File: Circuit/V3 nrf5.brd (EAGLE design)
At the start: 45.1 x 52.7 mm, 55 parts, among them J4 USB Micro, J7 CORTEX_DEBUG_SMD, Q2 BSS84, U2 MCP73831, U3 BC840M, U4 MIC5317 (MIC5205), U5 74AHCT2G125, U8 TPS61235P, Y2 FC-12M

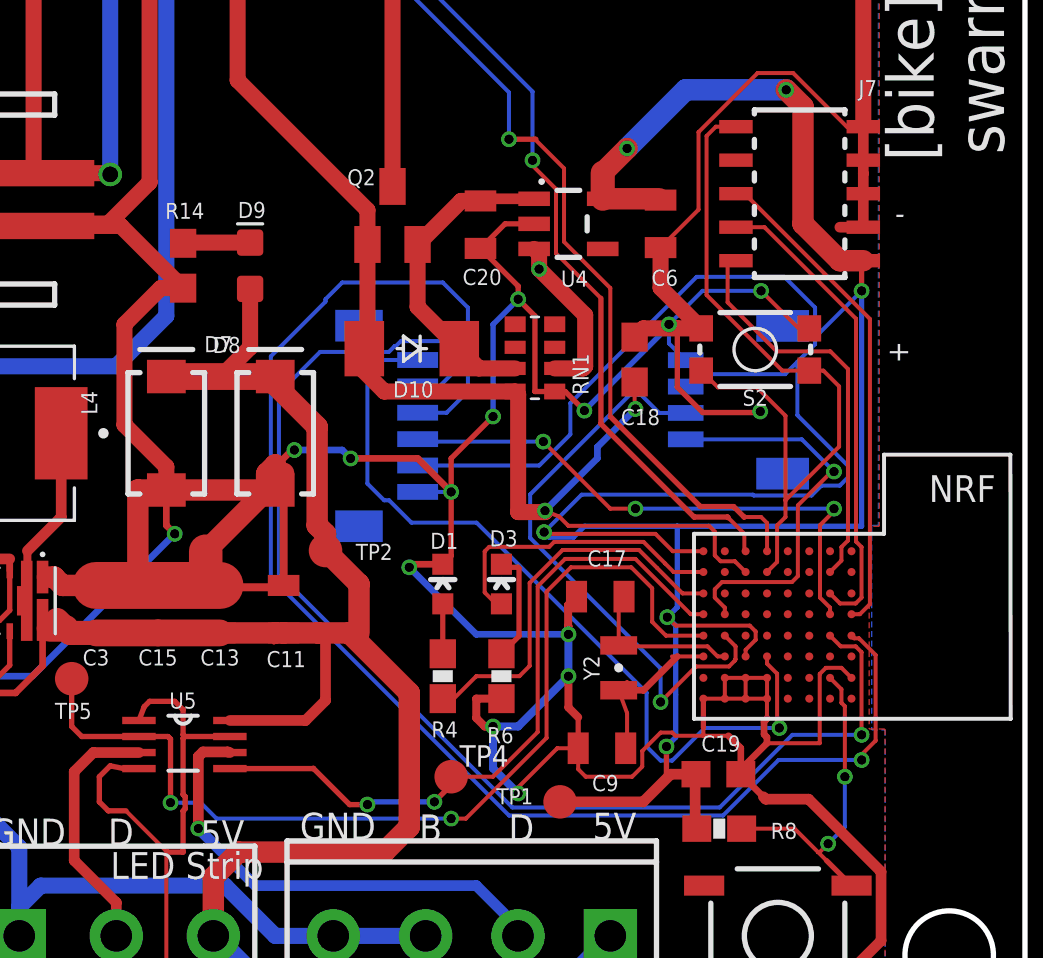
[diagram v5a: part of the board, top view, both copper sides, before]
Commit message: fix traces gnd
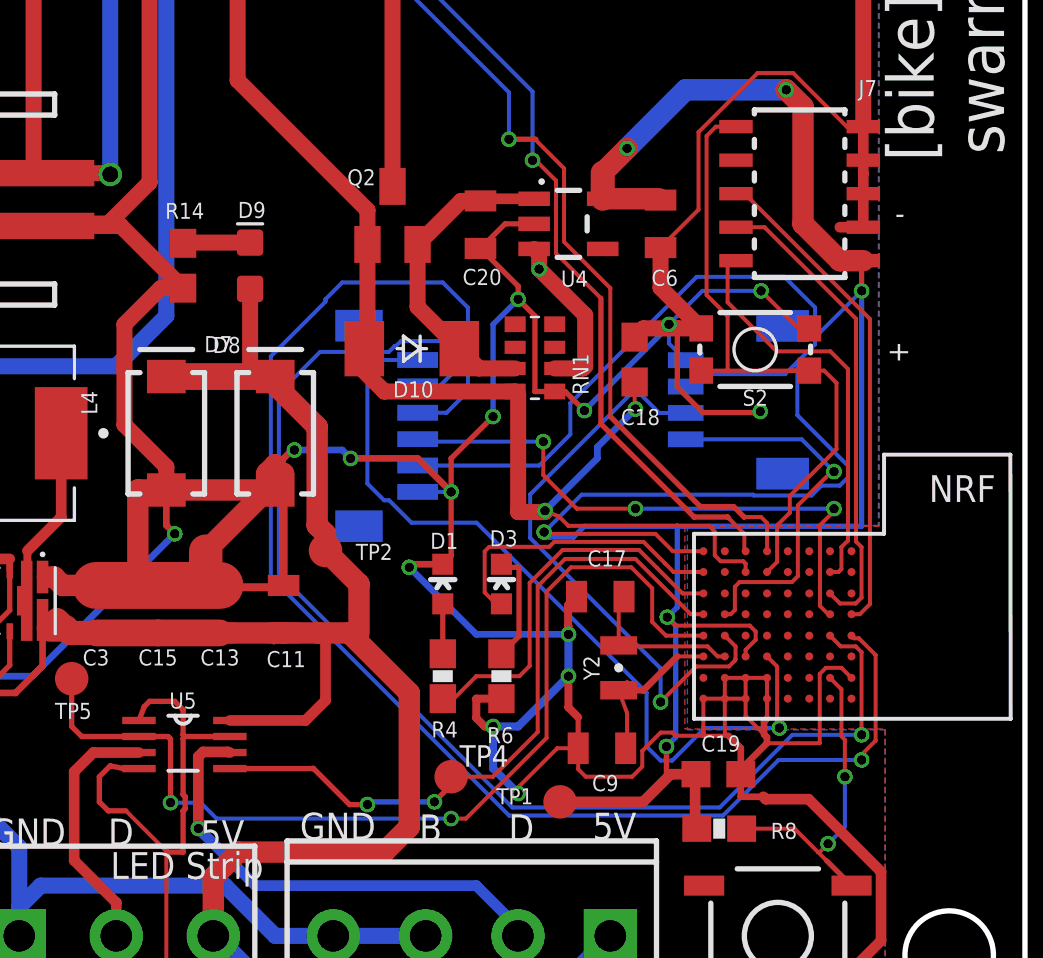
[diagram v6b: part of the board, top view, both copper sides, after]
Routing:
- net RESET: track 29.3 -> 24.8 mm
- net GND: track 338.8 -> 341.7 mm
- net PIN_01: track 21.4 -> 22.2 mm
- net 5V: track 90.5 -> 91.2 mm
- net SCL: track 15.6 -> 15.0 mm

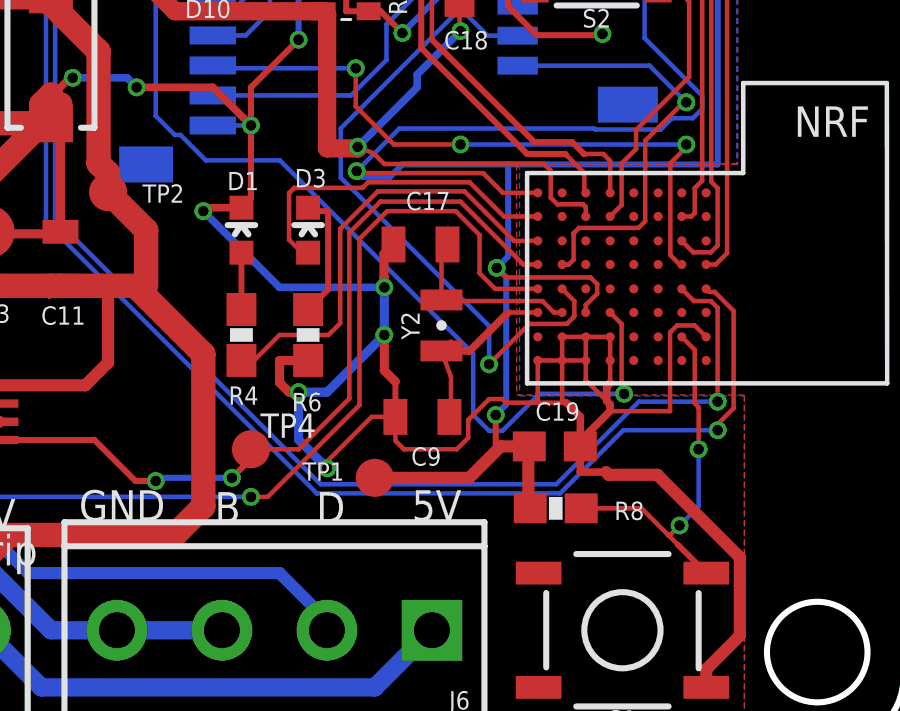
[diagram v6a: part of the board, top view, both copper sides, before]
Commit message: Moving to nrf52840-DK BSP pins for buttons and leds. Also driving LEDs with active LOW.
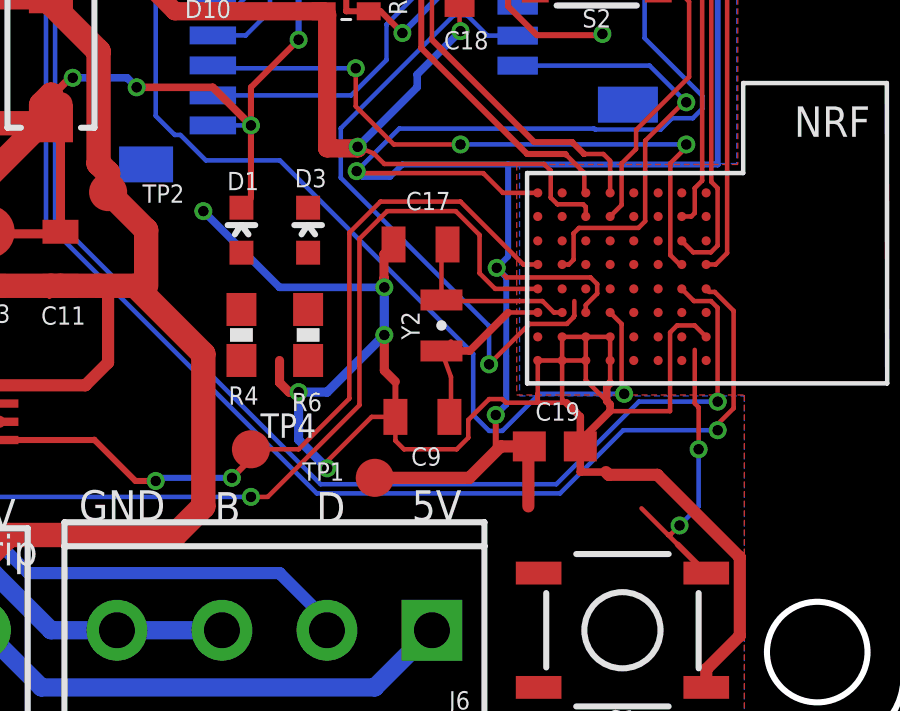
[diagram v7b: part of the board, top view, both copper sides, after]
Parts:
- removed R8: 10k, SparkFun:0603-RES
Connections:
- removed net N$7: D3.C, R6.2
- new net N$8: D3.A, R6.1
- net 3.3V: now also R4.1, R6.2; no longer R8.1
- net GND: no longer D1.C, R6.1
- net LED_1: now also D1.C, U3.D4; no longer R4.1, U3.C7
- net LED_2: now also D3.C, U3.C4; no longer D3.A, U3.B7
- net SWITCH_1: no longer R8.2, U3.G1
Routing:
- net LED_1: track 14.7 -> 0.00 mm
- net LED_2: track 11.3 -> 0.00 mm
- net N$7: track 4.25 -> 0.00 mm
- net SWITCH_1: track 12.4 -> 9.74 mm
- net GND: track 341.7 -> 339.1 mm
- net N$1: track 1.89 -> 0.00 mm
- net SDA: track 22.2 -> 21.7 mm
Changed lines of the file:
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@@
 <drawing>
 <settings>
-<setting alwaysvectorfont="no"/>
+<setting alwaysvectorfont="yes"/>
 <setting keepoldvectorfont="yes"/>
 <setting verticaltext="up"/>
@@
 <attribute name="VALUE" x="31.75" y="6.7945" size="0.6096" layer="27" font="vector" ratio="20" rot="R180" align="top-center"/>
 </element>
-<element name="R8" library="SparkFun" package="0603-RES" value="10k" x="29.5275" y="8.1915" smashed="yes">
-<attribute name="DIGIKEY" value="P10KGCT-ND" x="29.5275" y="8.1915" size="1.778" layer="27" display="off"/>
-<attribute name="NAME" x="32.48025" y="8.41375" size="0.6096" layer="25" font="vector" rot="R180"/>
-<attribute name="VALUE" x="28.5115" y="7.0485" size="0.4064" layer="27" font="vector"/>
-</element>
 <element name="U3" library="BC840M-v1" package="BC840M" value="BC840M" x="28.575" y="19.3675" smashed="yes" rot="R270">
 <attribute name="DIGIKEY" value="1914-BC840MCT-ND" x="28.575" y="19.3675" size="1.778" layer="27" rot="R270" display="off"/>
@@
 <contactref element="U3" pad="G0"/>
 <contactref element="C19" pad="2"/>
-<contactref element="D1" pad="C"/>
-<contactref element="R6" pad="1"/>
 <contactref element="C20" pad="2"/>
 <contactref element="RN1" pad="1"/>
@@
 <wire x1="20.6375" y1="12.065" x2="20.32" y2="12.3825" width="0.3048" layer="1"/>
 <wire x1="20.32" y1="13.12" x2="20.32" y2="12.3825" width="0.3048" layer="1"/>
-<wire x1="20.32" y1="13.12" x2="21.2725" y2="13.12" width="0.3048" layer="1"/>
 <wire x1="20.955" y1="12.065" x2="20.955" y2="10.4775" width="0.3048" layer="16"/>
 <wire x1="20.955" y1="10.4775" x2="21.9075" y2="9.525" width="0.3048" layer="16"/>
@@
 <wire x1="32.33053125" y1="36.83" x2="30.9822125" y2="36.83" width="0.1524" layer="1"/>
 <wire x1="30.9822125" y1="36.83" x2="28.7432" y2="34.5909875" width="0.1524" layer="1"/>
-<wire x1="19.05" y1="18.2125" x2="19.3675" y2="18.53" width="0.2032" layer="1"/>
 <wire x1="19.3675" y1="20.955" x2="19.3675" y2="18.53" width="0.2032" layer="1"/>
 <wire x1="19.3675" y1="20.955" x2="19.3675" y2="22.225" width="0.2032" layer="1"/>
@@
 <via x="17.78" y="18.0975" extent="1-16" drill="0.35"/>
 <wire x1="17.78" y1="18.0975" x2="17.895" y2="18.2125" width="0.254" layer="1"/>
-<wire x1="17.895" y1="18.2125" x2="19.05" y2="18.2125" width="0.254" layer="1"/>
 <wire x1="7.4931" y1="50.7752625" x2="7.4931" y2="51.05684375" width="0.254" layer="1"/>
 <wire x1="7.4931" y1="51.05684375" x2="6.16244375" y2="52.3875" width="0.254" layer="1"/>
@@
 <wire x1="29.7402" y1="13.1191" x2="29.7402" y2="11.8174" width="0.1524" layer="1"/>
 <wire x1="29.7402" y1="11.8174" x2="29.845" y2="11.7126" width="0.1524" layer="1"/>
+<wire x1="19.3675" y1="18.53" x2="17.895" y2="18.2125" width="0" layer="19" extent="1-1"/>
 </signal>
 <signal name="RESET">
@@
 <wire x1="30.4916125" y1="32.258" x2="35.2397" y2="27.5099125" width="0.1524" layer="1"/>
 <wire x1="35.2397" y1="27.5099125" x2="35.2397" y2="16.7009" width="0.1524" layer="1"/>
-</signal>
-<signal name="LED_1">
-<contactref element="U3" pad="C7"/>
-<contactref element="R4" pad="1"/>
-<wire x1="28.9274" y1="17.1069" x2="28.13685" y2="17.1069" width="0.1524" layer="1"/>
-<wire x1="28.13685" y1="17.1069" x2="27.1699" y2="18.07385" width="0.1524" layer="1"/>
-<wire x1="27.1699" y1="18.07385" x2="26.4891" y2="18.75465" width="0.1524" layer="1"/>
-<wire x1="26.4891" y1="18.75465" x2="23.59330625" y2="18.75465" width="0.1524" layer="1"/>
-<wire x1="23.59330625" y1="18.75465" x2="22.3421" y2="17.50344375" width="0.1524" layer="1"/>
-<wire x1="22.3421" y1="17.50344375" x2="22.3421" y2="14.35940625" width="0.1524" layer="1"/>
-<wire x1="21.95269375" y1="13.97" x2="20.32" y2="13.97" width="0.1524" layer="1"/>
-<wire x1="20.32" y1="13.97" x2="19.47" y2="13.12" width="0.1524" layer="1"/>
-<wire x1="19.47" y1="13.12" x2="19.05" y2="13.12" width="0.1524" layer="1"/>
-<wire x1="22.3421" y1="14.35940625" x2="21.95269375" y2="13.97" width="0.1524" layer="1"/>
 </signal>
 <signal name="STRIP_5V">
@@
 <signal name="SWITCH_1">
 <contactref element="S1" pad="3"/>
-<contactref element="R8" pad="2"/>
 <wire x1="33.5915" y1="6.985" x2="34.544" y2="6.0325" width="0.2" layer="1"/>
-<contactref element="U3" pad="G1"/>
 <wire x1="34.1598" y1="11.6912875" x2="34.29" y2="11.5610875" width="0.1524" layer="1"/>
-<wire x1="33.728" y1="13.9065" x2="34.1598" y2="13.4747" width="0.1524" layer="1"/>
 <wire x1="34.1598" y1="13.4747" x2="34.1598" y2="11.6912875" width="0.1524" layer="1"/>
 <wire x1="34.29" y1="11.5610875" x2="34.29" y2="10.16" width="0.1524" layer="1"/>
 <via x="34.29" y="10.16" extent="1-16" drill="0.35"/>
-<wire x1="30.3775" y1="8.1915" x2="32.385" y2="8.1915" width="0.1524" layer="1"/>
 <wire x1="32.385" y1="8.1915" x2="33.274" y2="7.3025" width="0.1524" layer="1"/>
 <wire x1="33.274" y1="7.3025" x2="33.5915" y2="6.985" width="0.1524" layer="1"/>
@@
 </signal>
 <signal name="LED_2">
-<contactref element="D3" pad="A"/>
-<contactref element="U3" pad="B7"/>
-<wire x1="28.9274" y1="17.9197" x2="27.8003" y2="17.9197" width="0.1524" layer="1"/>
-<wire x1="27.8003" y1="17.9197" x2="27.4747" y2="18.2453" width="0.1524" layer="1"/>
-<wire x1="27.4747" y1="18.2453" x2="26.66055" y2="19.05945" width="0.1524" layer="1"/>
-<wire x1="26.66055" y1="19.05945" x2="23.2705875" y2="19.05945" width="0.1524" layer="1"/>
-<wire x1="20.8095625" y1="18.87285" x2="20.6375" y2="18.7007875" width="0.1524" layer="1"/>
-<wire x1="20.6375" y1="18.7007875" x2="20.6375" y2="17.145" width="0.1524" layer="1"/>
-<wire x1="23.2705875" y1="19.05945" x2="23.0839875" y2="18.87285" width="0.1524" layer="1"/>
-<wire x1="23.0839875" y1="18.87285" x2="20.8095625" y2="18.87285" width="0.1524" layer="1"/>
-<wire x1="20.6375" y1="17.145" x2="21.07" y2="16.7125" width="0.1524" layer="1"/>
-<wire x1="21.07" y1="16.7125" x2="21.2725" y2="16.7125" width="0.1524" layer="1"/>
+<contactref element="D3" pad="C"/>
+<contactref element="U3" pad="C4"/>
+<wire x1="21.2725" y1="18.2125" x2="31.3404" y2="17.1069" width="0" layer="19" extent="1-1"/>
 </signal>
 <signal name="VBUS">
@@
 <contactref element="U4" pad="5"/>
 <contactref element="C6" pad="1"/>
-<contactref element="R8" pad="1"/>
 <contactref element="TP1" pad="TP"/>
 <contactref element="U3" pad="A7"/>
@@
 <wire x1="27.8765" y1="11.65225" x2="27.52725" y2="11.303" width="0.2032" layer="16"/>
 <wire x1="28.614" y1="10.2235" x2="28.614" y2="8.255" width="0.4064" layer="1"/>
-<wire x1="28.614" y1="8.255" x2="28.6775" y2="8.1915" width="0.4064" layer="1"/>
 <contactref element="J5" pad="2"/>
 <contactref element="J2" pad="2"/>
@@
 <wire x1="32.4894" y1="25.8811125" x2="32.4894" y2="23.8637" width="0.1524" layer="16"/>
 <wire x1="32.4894" y1="23.8637" x2="34.40785" y2="21.94525" width="0.1524" layer="16"/>
-</signal>
-<signal name="N$1">
-<contactref element="R4" pad="2"/>
-<contactref element="D1" pad="A"/>
-<wire x1="19.05" y1="14.82" x2="19.05" y2="16.7125" width="0.2" layer="1"/>
-</signal>
-<signal name="N$7">
+<contactref element="R4" pad="1"/>
 <contactref element="R6" pad="2"/>
-<contactref element="D3" pad="C"/>
-<wire x1="21.2725" y1="18.2125" x2="21.3875" y2="18.0975" width="0.2" layer="1"/>
-<wire x1="21.3875" y1="18.0975" x2="21.9075" y2="18.0975" width="0.2" layer="1"/>
-<wire x1="21.9075" y1="18.0975" x2="21.93925" y2="18.06575" width="0.2" layer="1"/>
-<wire x1="21.93925" y1="15.48675" x2="21.2725" y2="14.82" width="0.2" layer="1"/>
-<wire x1="21.93925" y1="18.06575" x2="21.93925" y2="15.48675" width="0.2" layer="1"/>
+<wire x1="19.05" y1="13.12" x2="21.2725" y2="14.82" width="0" layer="19" extent="1-1"/>
+<wire x1="22.89175" y1="19.431" x2="21.2725" y2="14.82" width="0" layer="19" extent="1-1"/>
 </signal>
 <signal name="N$4">
@@
 <signal name="SDA">
 <contactref element="J5" pad="3"/>
-<contactref element="U3" pad="E6"/>
 <wire x1="26.5722875" y1="24.62885" x2="26.1327125" y2="24.62885" width="0.1524" layer="16"/>
 <wire x1="22.36115" y1="19.2112125" x2="27.305" y2="14.2673625" width="0.1524" layer="16"/>
@@
 <wire x1="27.305" y1="14.2673625" x2="27.305" y2="12.9919" width="0.1524" layer="16"/>
 <wire x1="30.1466" y1="14.605" x2="30.1466" y2="15.1003" width="0.1524" layer="1"/>
-<wire x1="30.1466" y1="15.1003" x2="29.7402" y2="15.5067" width="0.1524" layer="1"/>
 <wire x1="28.2575" y1="23.9475" x2="27.2536375" y2="23.9475" width="0.1524" layer="16"/>
 <wire x1="27.2536375" y1="23.9475" x2="26.5722875" y2="24.62885" width="0.1524" layer="16"/>
+<contactref element="U3" pad="E6"/>
+<wire x1="30.1466" y1="15.1003" x2="29.7402" y2="15.5067" width="0" layer="19" extent="1-1"/>
 </signal>
 <signal name="SCL">
@@
 <wire x1="31.7214" y1="12.0936" x2="31.80769375" y2="12.00730625" width="0.1524" layer="1"/>
 </signal>
+<signal name="N$1">
+<contactref element="R4" pad="2"/>
+<contactref element="D1" pad="A"/>
+<wire x1="19.05" y1="14.82" x2="19.05" y2="16.7125" width="0" layer="19" extent="1-1"/>
+</signal>
+<signal name="LED_1">
+<contactref element="D1" pad="C"/>
+<contactref element="U3" pad="D4"/>
+<wire x1="19.05" y1="18.2125" x2="31.3404" y2="16.3195" width="0" layer="19" extent="1-1"/>
+</signal>
+<signal name="N$8">
+<contactref element="R6" pad="1"/>
+<contactref element="D3" pad="A"/>
+<wire x1="21.2725" y1="13.12" x2="21.2725" y2="16.7125" width="0" layer="19" extent="1-1"/>
+</signal>
 </signals>

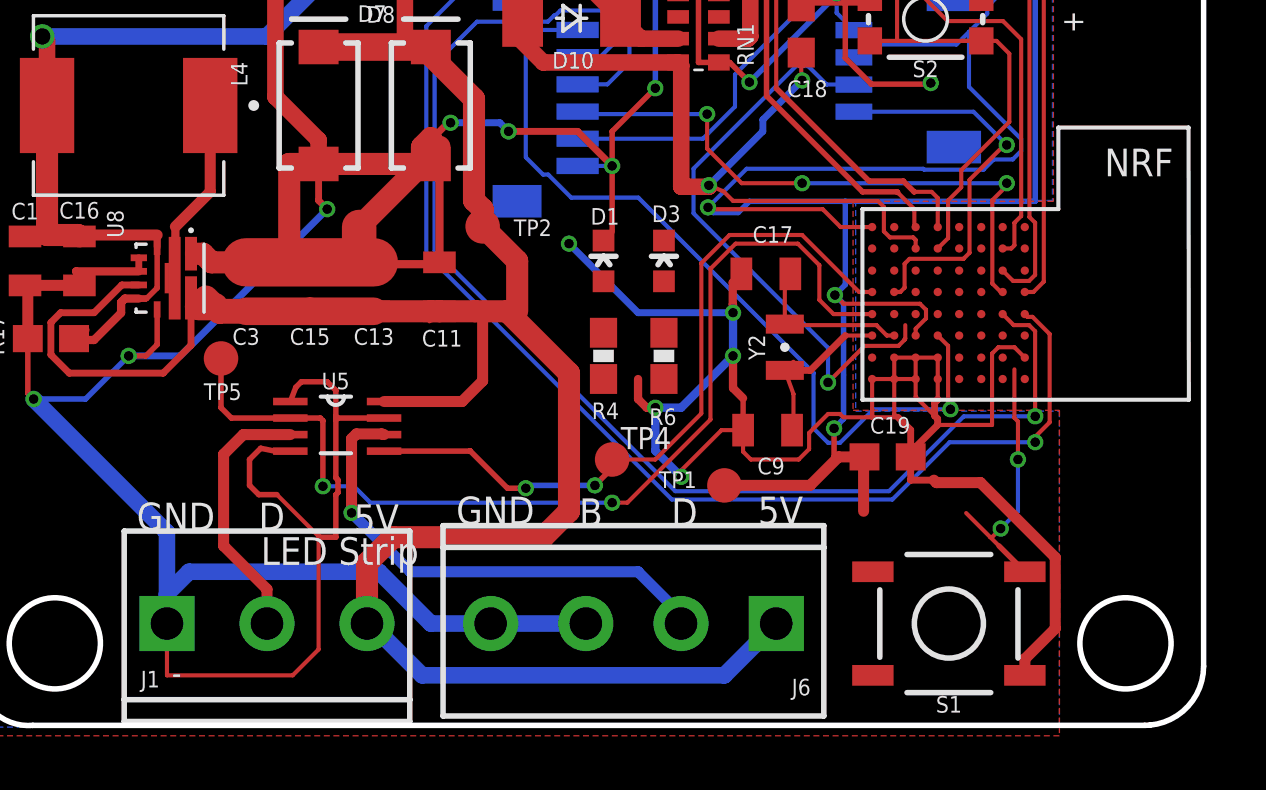
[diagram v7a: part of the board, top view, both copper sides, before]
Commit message: Adding debugging pins for switch and leds.
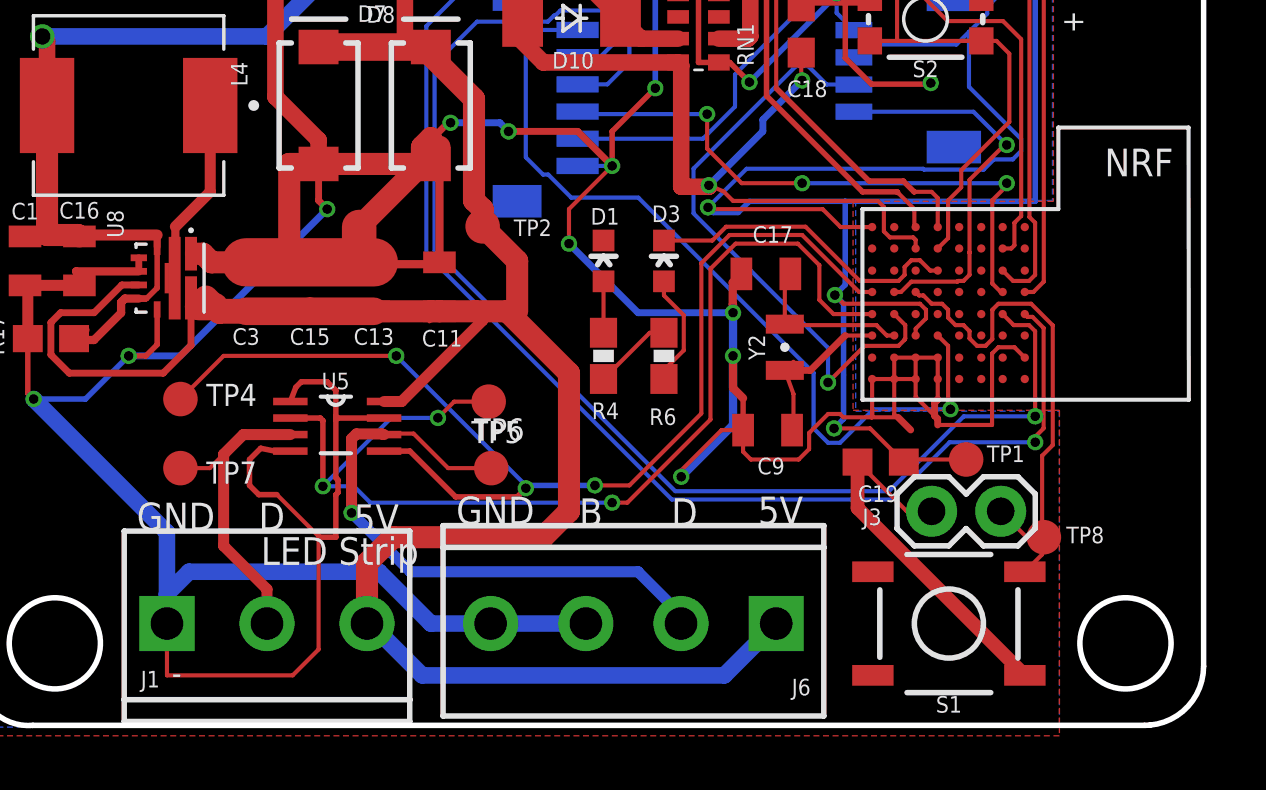
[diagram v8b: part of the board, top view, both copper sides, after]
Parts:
- added J3: (no value), SparkFun-Connectors:1X02
- added TP6, TP7, TP8: TPSB1,27, testpad:B1,27
- moved TP4 16.0 mm to (3.49, 12.4)
- moved TP5 9.97 mm to (14.8, 12.3)
- moved TP1 8.94 mm to (32.4, 10.2)
- moved C19 0.32 mm to (29.2, 10.1), turned to 180 degrees
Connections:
- removed net CTRL_CH1: U3.A3
- removed net CTRL_CH2: U3.A2
- removed net CTRL_CH3: U3.A1
- net GND: now also J3.1
- net HEADLAMP_5V: now also TP7.TP
- net STRIP_5V: now also TP6.TP
- net SWITCH_1: now also J3.2, TP8.TP, U3.D5
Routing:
- net HEADLAMP_3V3: track 26.9 -> 42.7 mm, vias 2 -> 3
- net LED_2: track 0.00 -> 11.7 mm
- net SWITCH_1: track 9.74 -> 19.3 mm, vias 2 -> 0
- net STRIP_5V: track 18.0 -> 22.5 mm
- net N$8: track 0.00 -> 4.20 mm
- net STRIP_3V3: track 37.6 -> 40.5 mm, vias 2 -> 3
- net GND: track 339.1 -> 336.7 mm, vias 18 -> 17
- net N$1: track 0.00 -> 1.89 mm
- net HEADLAMP_5V: track 9.64 -> 11.4 mm
- net 3.3V: track 117.8 -> 116.4 mm
- net 5V: track 91.2 -> 89.9 mm
- net SDA: track 21.7 -> 22.2 mm
